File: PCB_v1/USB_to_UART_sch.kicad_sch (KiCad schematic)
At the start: 10 parts, among them IC3 FT2332RL

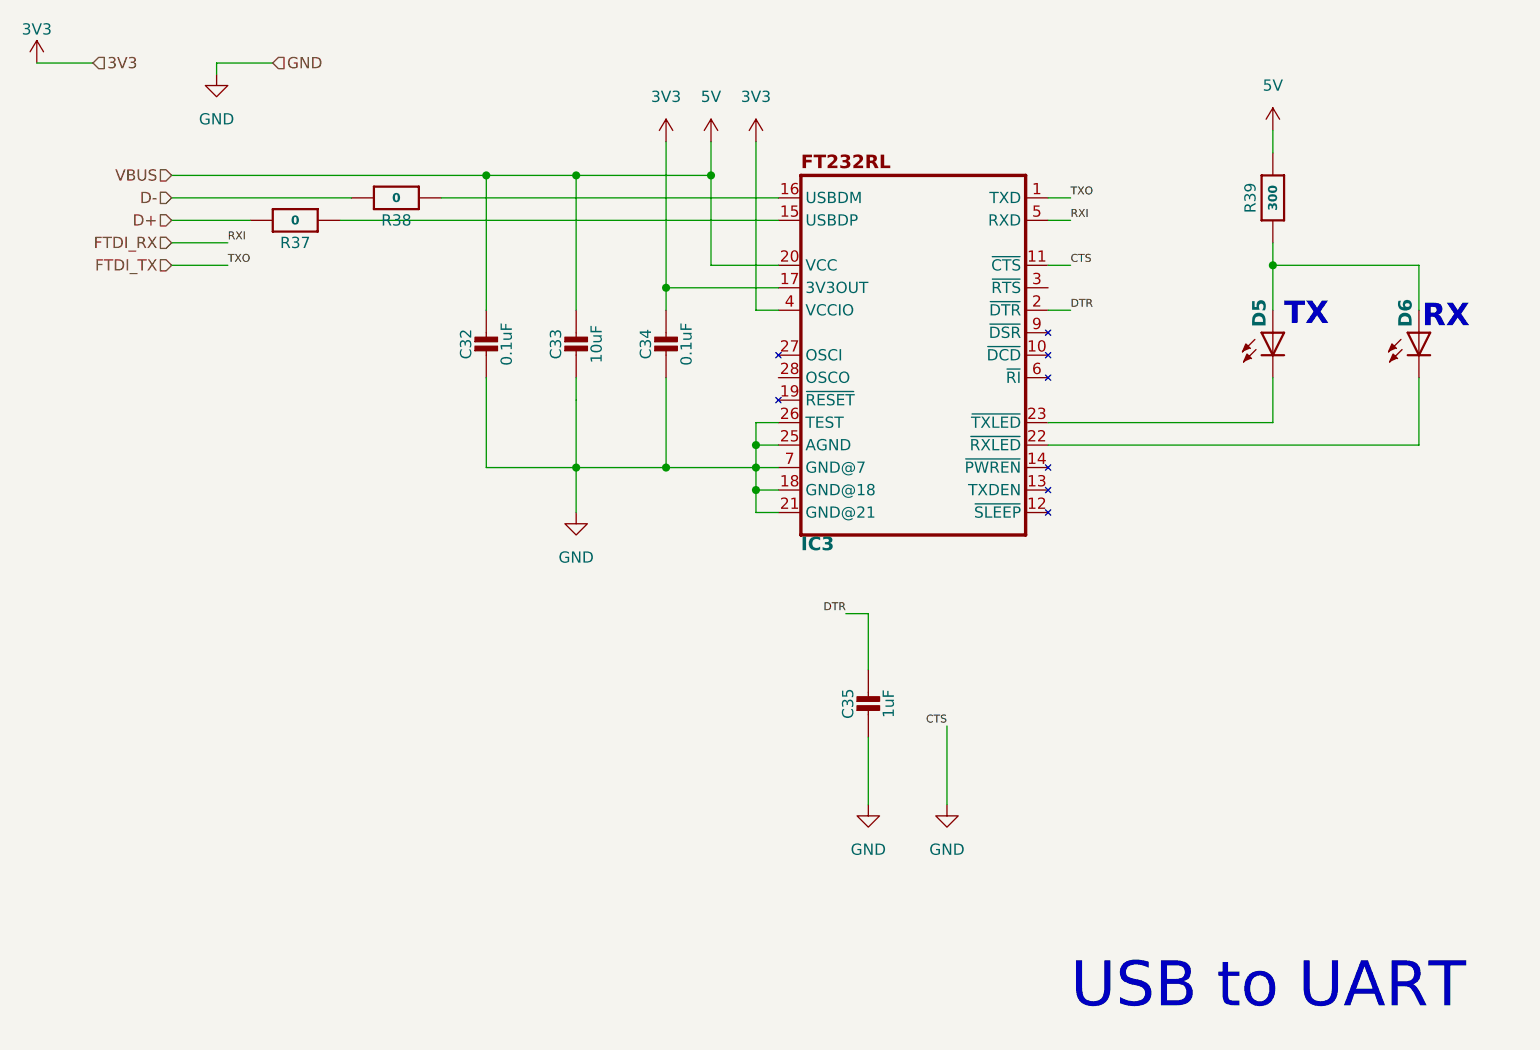
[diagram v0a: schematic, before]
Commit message: adding the parts library
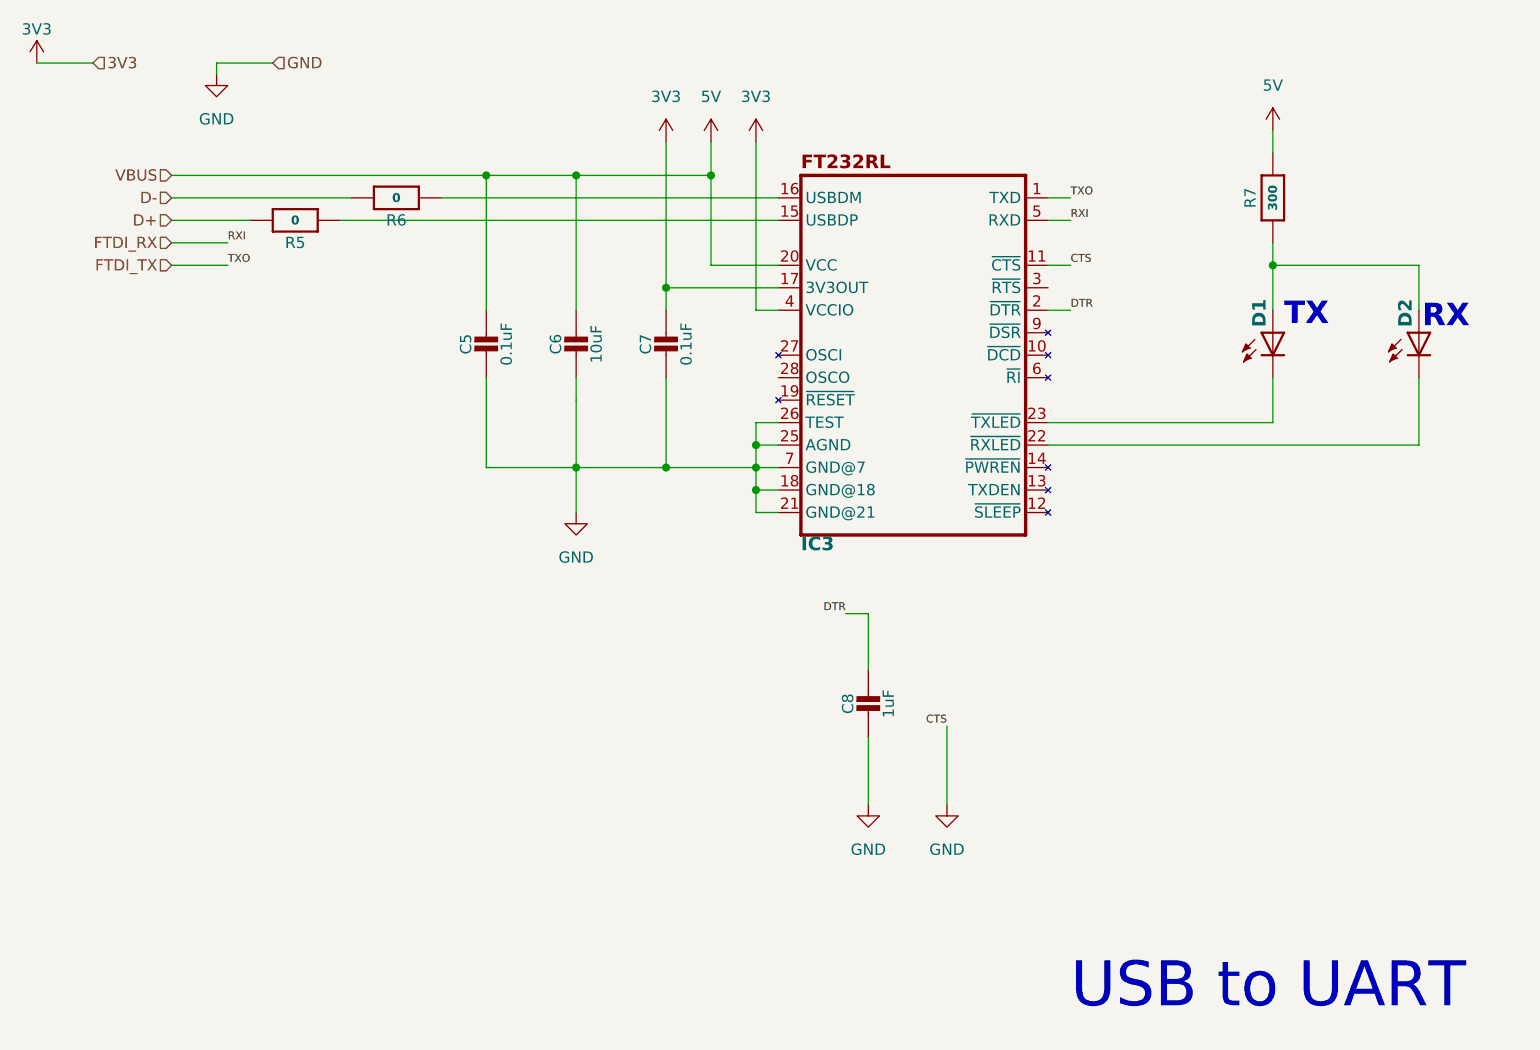
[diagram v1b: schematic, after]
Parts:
- C5: renamed from C32; footprint 0603-NO -> Capacitor_SMD:C_0805_2012Metric
- C6: renamed from C33; footprint 0603-NO -> Capacitor_SMD:C_0805_2012Metric
- C7: renamed from C34; footprint 0603-NO -> Capacitor_SMD:C_0805_2012Metric
- C8: renamed from C35; footprint 0603-NO -> Capacitor_SMD:C_0805_2012Metric
- D1: renamed from D5; footprint LED-0603 -> LED_SMD:LED_0805_2012Metric_Pad1.15x1.40mm_HandSolder
- D2: renamed from D6; footprint LED-0603 -> LED_SMD:LED_0805_2012Metric_Pad1.15x1.40mm_HandSolder
- R5: renamed from R37; footprint 0603-NO -> Resistor_SMD:R_0805_2012Metric
- R6: renamed from R38; footprint 0603-NO -> Resistor_SMD:R_0805_2012Metric
- R7: renamed from R39; footprint 0603-NO -> Resistor_SMD:R_0805_2012Metric
